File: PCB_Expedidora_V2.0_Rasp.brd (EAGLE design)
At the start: 99.1 x 62.2 mm, 37 parts, among them K2 G5L, T2 2N2222

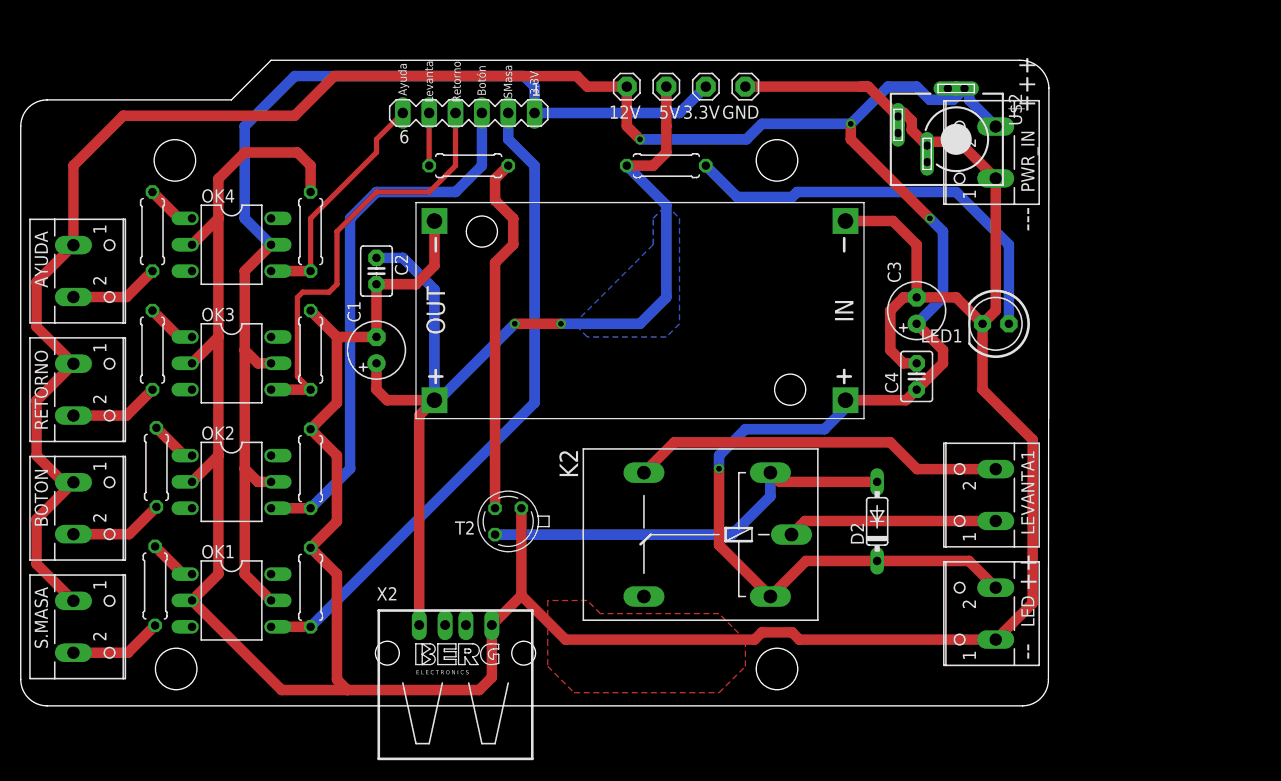
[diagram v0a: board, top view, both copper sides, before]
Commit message: V2.1
Agrego botones y cambio de posición las borneras
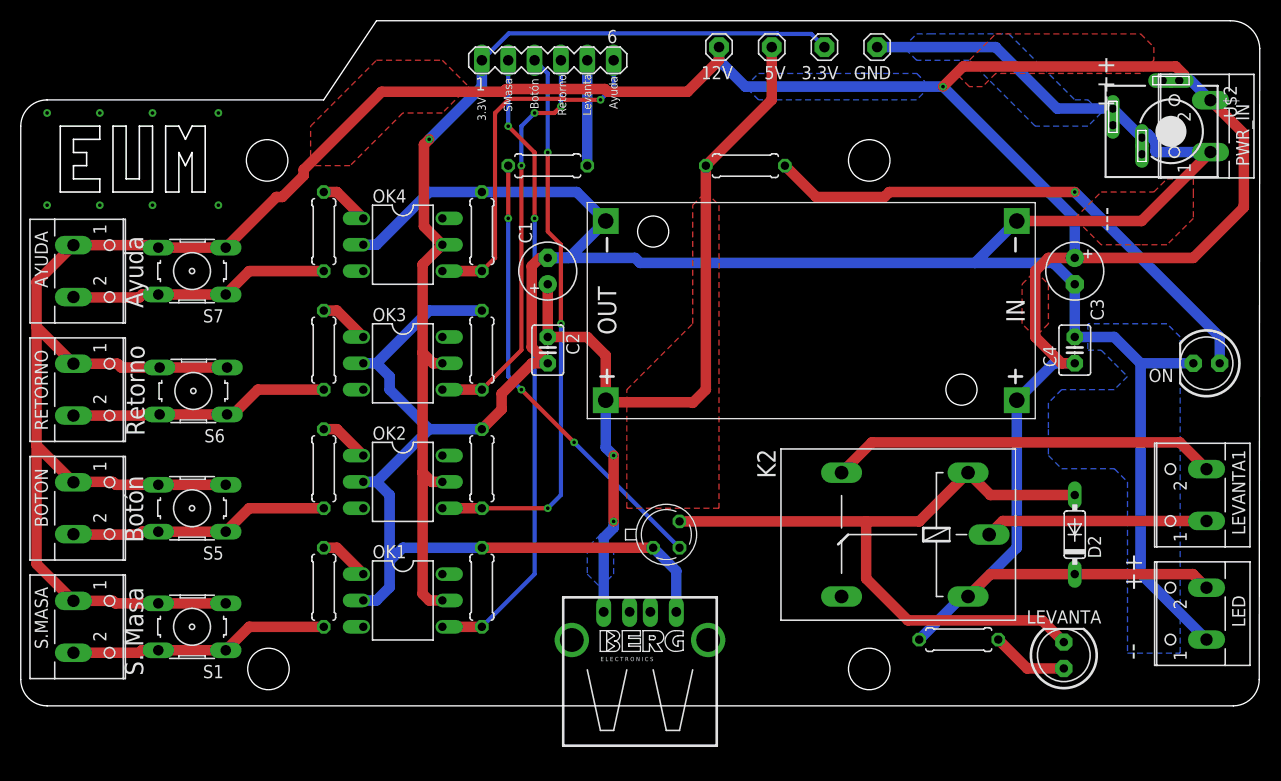
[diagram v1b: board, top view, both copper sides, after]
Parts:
- removed LED1: (no value), adafruit:LED5MM
- removed X2: (no value), con-berg:PN87520
- added LEVANTA, ON: (no value), adafruit:LED5MM
- added R7: 560, rcl:0207/7
- added S1, S5, S6, S7: (no value), switch-omron:B3F-10XX
- added X3: PN87520-S, con-berg:PN87520-S
- R12, R2, R4, R6: value 10k -> 100k
- moved PWR_IN 20.9 mm to (113.4, 55.9)
- moved U$2 20.7 mm to (110.9, 55.4)
- moved LED 20.3 mm to (113.0, 8.89)
- moved LEVANTA1 20.3 mm to (113.0, 20.3)
- moved D2 19.1 mm to (101.6, 16.5)
- moved K2 19.0 mm to (83.8, 16.5)
- moved C1 18.2 mm to (50.8, 41.9)
- moved C2 18.2 mm to (50.8, 34.3)
- moved U$1 16.5 mm to (76.2, 38.1)
- moved R11 16.5 mm to (29.2, 45.7)
- moved R12 16.5 mm to (44.5, 45.7)
- moved R2 16.5 mm to (44.5, 11.4)
- moved R4 16.5 mm to (44.5, 22.9)
- moved R5 16.5 mm to (29.2, 34.3)
- moved R6 16.5 mm to (44.5, 34.3)
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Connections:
- removed net N$17: D2.A, K2.1, T2.3
- new net LED_IND: D2.A, K2.1, LEVANTA.K, T2.3
- new net N$5: LEVANTA.A, R7.1
- net +12V: now also R7.2, S1.3, S1.4, S5.3, S5.4, S6.3, S6.4, S7.3, S7.4
- net +5V: now also X3.1; no longer X2.1
- net GND: now also ON.K, X3.4; no longer LED1.K, X2.4
- net N$1: now also S1.1, S1.2
- net N$13: now also ON.A; no longer LED1.A
- net N$2: now also S5.1, S5.2
- net N$6: now also S6.1, S6.2
- net N$9: now also S7.1, S7.2
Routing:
- net +12V: track 247.8 -> 341.7 mm, vias 4 -> 1
- net LED_IND: track 0.00 -> 68.0 mm
- net N$17: track 41.0 -> 0.00 mm, vias 0 -> 1
- net GND: track 333.0 -> 301.0 mm
- net N$1: track 8.96 -> 34.3 mm
- net +5V: track 99.8 -> 83.2 mm
- net N$9: track 8.66 -> 25.2 mm
- net N$6: track 8.66 -> 25.2 mm
- net N$2: track 9.09 -> 25.2 mm
- net AYUDA: track 22.7 -> 34.7 mm, vias 0 -> 1
- net N$13: track 40.4 -> 51.7 mm, vias 0 -> 1
- net +3V3: track 105.5 -> 96.7 mm, vias 0 -> 1
- net N$18: track 35.0 -> 43.7 mm, vias 0 -> 3
- net N$5: track 0.00 -> 7.47 mm
- net LEVANTA: track 5.08 -> 10.2 mm
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- added copper zone on layer 1, net +12V
- added copper zone on layer 16, net +12V
- added copper zone on layer 1, net +5V
- added copper zone on layer 16, net GND
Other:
- board size 99.1 x 62.2 mm -> 119.4 x 66 mm
- board text added: "No. Serie"
- board text added: "QC"
- board text added: "S. Masa"
